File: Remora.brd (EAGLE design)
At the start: 86.4 x 66.7 mm, 81 parts, among them IC1 MCP23017, J2 GROVE-I2C, P1 PADSMALL, T1 2N3904, T2 BSS138

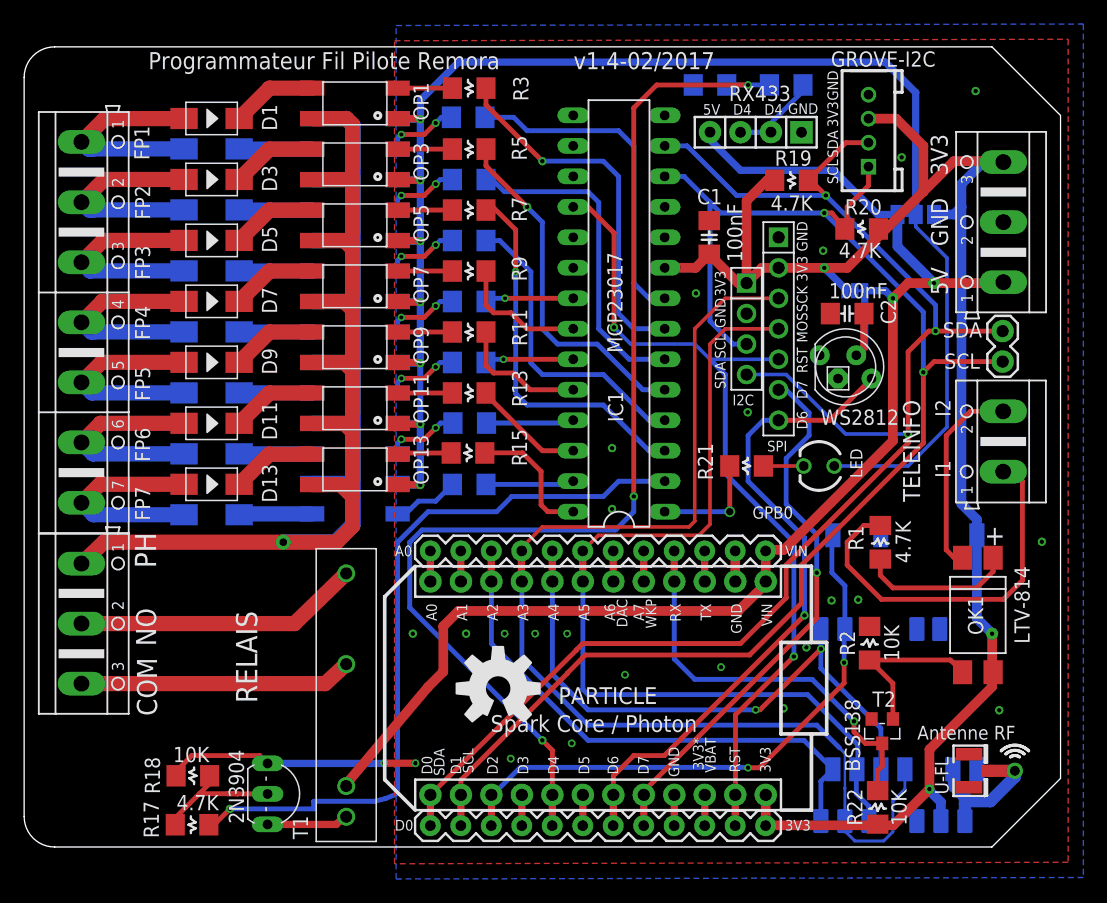
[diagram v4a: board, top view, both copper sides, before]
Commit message: Modification de la Remora pour accepter directement un Wemos D1 mini sur headers
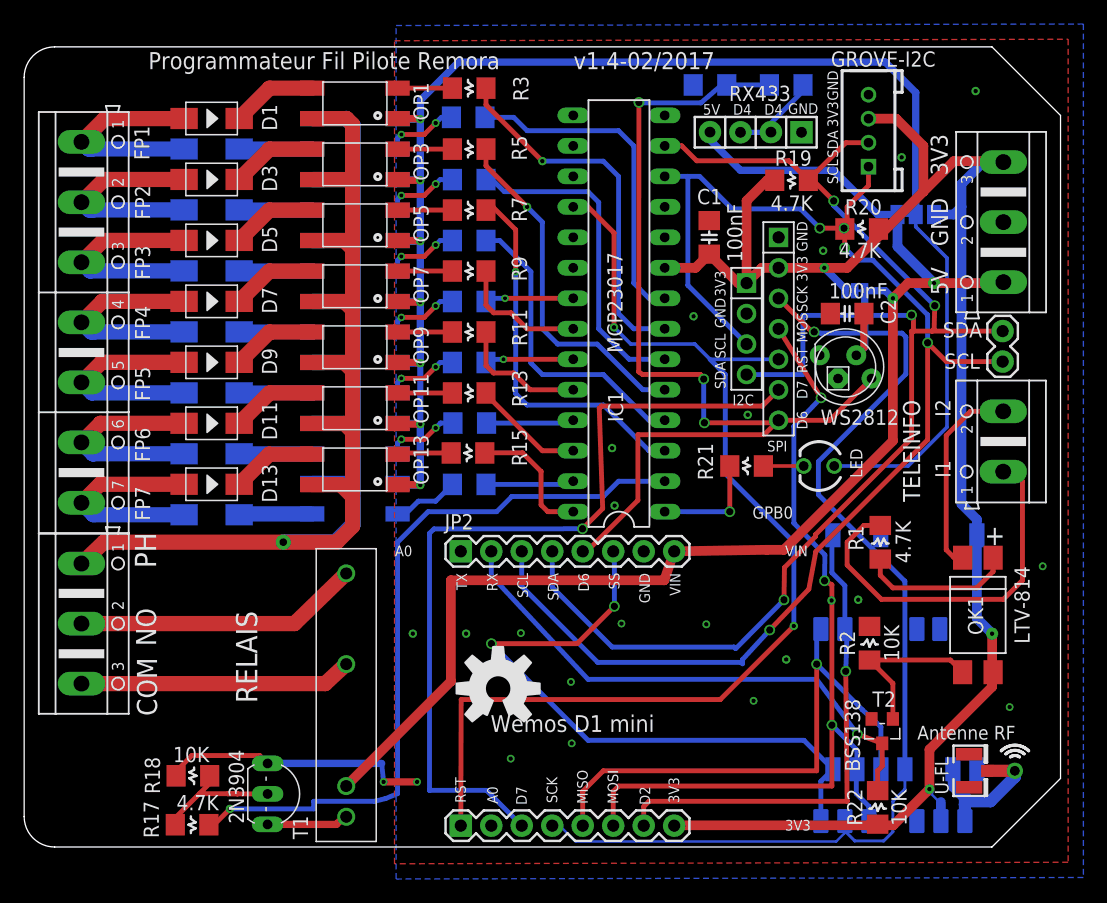
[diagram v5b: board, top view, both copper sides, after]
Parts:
- removed JP3, JP4: M12PTH, Spark:1X12-SMALL-PADS
- removed PARTICLE: Spark/Photon, Spark:SPARK_CORE
- added JP2: JP2, SparkFun:1X08
- added JP5: JP5, SparkFun:1X08
- PH: value (none) -> Ph
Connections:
- removed net A1: JP3.2, PARTICLE.11
- removed net A6/DAC: JP3.7, PARTICLE.6
- removed net A7/WKP: JP3.8, PARTICLE.5
- removed net D2: JP4.3, PARTICLE.15, U$2.IRQ, U$3.DIO0
- removed net D4: JP4.5, PARTICLE.17, R23.2, R24.1
- removed net D5: JP4.6, PARTICLE.18
- removed net D6: JP4.7, PARTICLE.19, SPI_OLED.7, WS2812.1
- removed net D7: JP4.8, PARTICLE.20, SPI_OLED.6
- removed net VDDA: JP4.10, PARTICLE.22
- new net D0: JP5.3, SPI_OLED.6
- new net D8: JP5.7, U$2.IRQ, U$3.DIO0
- net +3V3: now also JP5.8; no longer JP4.12, PARTICLE.24
- net +5V: now also JP2.8; no longer JP3.12, PARTICLE.1
- net A0: now also JP5.2; no longer JP3.1, PARTICLE.12
- net D3: now also JP2.5, R23.2, R24.1, SPI_OLED.7, WS2812.1; no longer JP4.4, PARTICLE.16
- net GND: now also JP2.7; no longer JP3.11, JP4.9, PARTICLE.2, PARTICLE.21
- net MISO: now also JP5.5; no longer JP3.5, PARTICLE.8
- net MOSI: now also JP5.6; no longer JP3.6, PARTICLE.7
- net RST: now also JP5.1; no longer JP4.11, PARTICLE.23
- net RX: now also JP2.2; no longer JP3.9, PARTICLE.4
- net SCK: now also JP5.4; no longer JP3.4, PARTICLE.9
- net SCL: now also JP2.3; no longer JP4.2, PARTICLE.14
- net SDA: now also JP2.4; no longer JP4.1, PARTICLE.13
- net SS: now also JP2.6; no longer JP3.3, PARTICLE.10
- net TX: now also JP2.1; no longer JP3.10, PARTICLE.3
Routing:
- net D4: track 95.8 -> 0.00 mm, vias 3 -> 0
- net D3: track 2.58 -> 82.7 mm, vias 0 -> 3
- net D0: track 0.00 -> 69.6 mm, vias 0 -> 1
- net D6: track 54.8 -> 0.00 mm, vias 1 -> 0
- net D2: track 48.7 -> 0.00 mm, vias 2 -> 0
- net D7: track 45.6 -> 0.00 mm, vias 1 -> 0
- net D8: track 0.00 -> 41.5 mm, vias 0 -> 1
- net RST: track 70.8 -> 92.9 mm
- net RX: track 33.9 -> 44.9 mm
- net SDA: track 126.5 -> 117.4 mm, vias 3 -> 4
- net SS: track 45.3 -> 53.7 mm, vias 0 -> 2
- net SCK: track 96.8 -> 90.4 mm, vias 0 -> 1
- net SCL: track 122.1 -> 115.9 mm, vias 2 -> 5
- net +3V3: track 138.9 -> 144.1 mm
- net MOSI: track 76.1 -> 72.0 mm, vias 0 -> 3
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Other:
- board text added: "MISO"
- board text added: "MOSI"
- board text added: "SS"
- board text added: "Wemos D1 mini"
- board text removed: "3V3*"
- board text removed: "A1"
- board text removed: "A2"
- board text removed: "A3"
- board text removed: "A4"
- board text removed: "A5"
- board text removed: "A6"
- board text removed: "A7"
- board text removed: "D0"
- board text removed: "D1"
- board text removed: "D3"
- board text removed: "D5"
- board text removed: "DAC"
- board text removed: "Spark Core / Photon"
- board text removed: "VBAT"
- board text removed: "WKP"

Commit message: Mise à jour du numéro de version du PCB
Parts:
- PH: value Ph -> (none)
- moved JP2 2.54 mm to (38.9, 24.6)
- moved JP5 2.54 mm to (38.9, 1.78)
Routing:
- net SS: track 53.7 -> 37.2 mm
- net SCK: track 90.4 -> 97.5 mm
- net D3: track 82.7 -> 77.1 mm
- net RST: track 92.9 -> 88.3 mm
- net +3V3: track 144.1 -> 140.8 mm
- net D0: track 69.6 -> 72.2 mm
- net D8: track 41.5 -> 39.2 mm
- net MISO: track 46.4 -> 44.9 mm
- net MOSI: track 72.0 -> 70.8 mm
- net SDA: track 117.4 -> 116.9 mm, vias 4 -> 6
- net SCL: track 115.9 -> 116.3 mm, vias 5 -> 3
- net GND: track 23.2 -> 23.3 mm, vias 23 -> 32
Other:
- board text added: "D0"
- board text added: "D3"
- board text added: "D8"
- board text added: "v1.5-02/2017"
- board text removed: "D2"
- board text removed: "v1.4-02/2017"
